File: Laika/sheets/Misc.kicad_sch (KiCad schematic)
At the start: 0 parts

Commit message: Created misc. block
Populated sheet for misc. components. This includes three switches for
SoC bringup (update, reset, arm/risc-v select). Added buzzer and user
led.
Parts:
- added BZ1: Buzzer, symbol Device:Buzzer
- added C10, C9: C, symbol Device:C
- added D4, D5, D7: D_TVS, symbol Device:D_TVS
- added D6: D, symbol Device:D
- added D8: LED, symbol Device:LED
- added Q1: Q_NPN, symbol Device:Q_NPN
- added Q2: Q_NMOS, symbol Device:Q_NMOS
- added R10, R13, R14, R8: 10k, symbol Device:R
- added R11: 180, symbol Device:R
- added R12, R7, R9: 100, symbol Device:R
- added R15, R16: 1k, symbol Device:R
- added SW1, SW2: SW_Push, symbol Switch:SW_Push
- added SW3: SW_DPDT_x2, symbol Switch:SW_DPDT_x2
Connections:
- new net: D5.2 (A2), R9.1, SW2.2
- new net: Q1.B, R11.2
- new net: BZ1.2 (-), D6.2 (A), Q1.C
- new net: R14.2, SW3.1 (A)
- new net: D7.2 (A2), R12.2, SW3.2 (B)
- new net: R13.1, SW3.3 (C)
- new net: D8.1 (K), Q2.D
- new net: Q2.G, R16.1
- new net: D4.2 (A2), R7.1, SW1.2
- new net: D8.2 (A), R15.1
- new net +1V8: R10.2, R14.1, R8.2
- new net +3V3: BZ1.1 (+), D6.1 (K), R15.2
- new net AARCH_SEL: R12.1
- new net BUZZER: R11.1
- new net GND: C10.2, C9.2, D4.1 (A1), D5.1 (A1), D7.1 (A1), Q1.E, Q2.S, R13.2, SW1.1, SW2.1
- new net RESET: C10.1, R10.1, R9.2
- new net UPDATE: C9.1, R7.2, R8.1
- new net USER_LED: R16.2
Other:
- note added: "Arm/RISC-V Switch"
- note added: "Blue PWR LED"
- note added: "Buzzer"
- note added: "Miscellaneous"
- note added: "Reset"
- note added: "USB Update Mode"
- note added: "User LED"

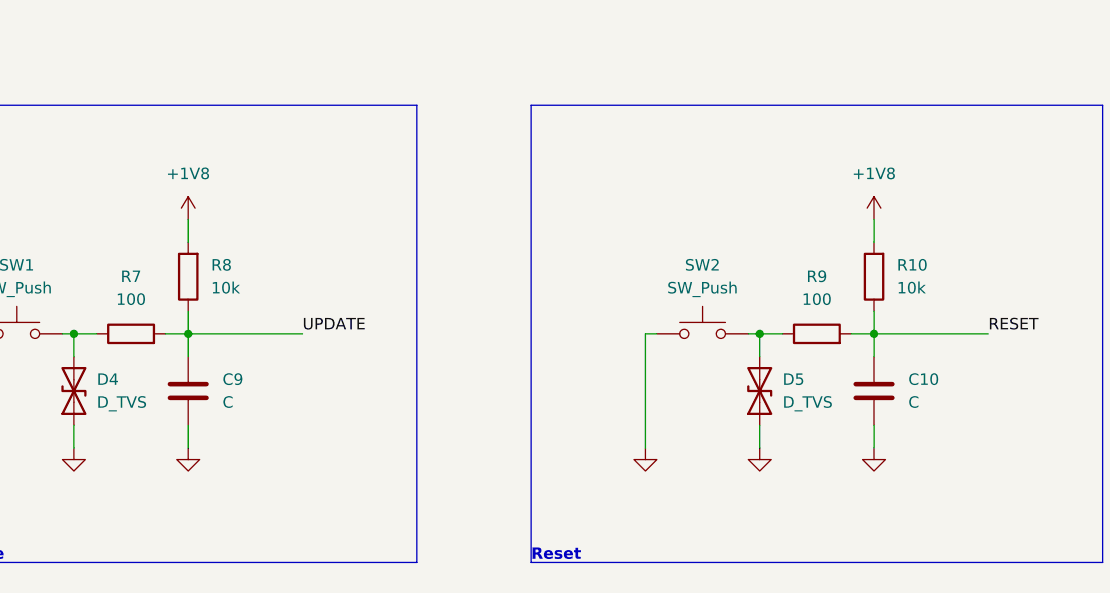
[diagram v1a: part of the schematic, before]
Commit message: Fixed reset block and added VDD_VBAT
Fixed the reset circuit to instead be pulled up to the 3v3 reg using a
voltage divider for 1.8v. RTC power (VDD_BAT) is provided by the 3v3
regulator.
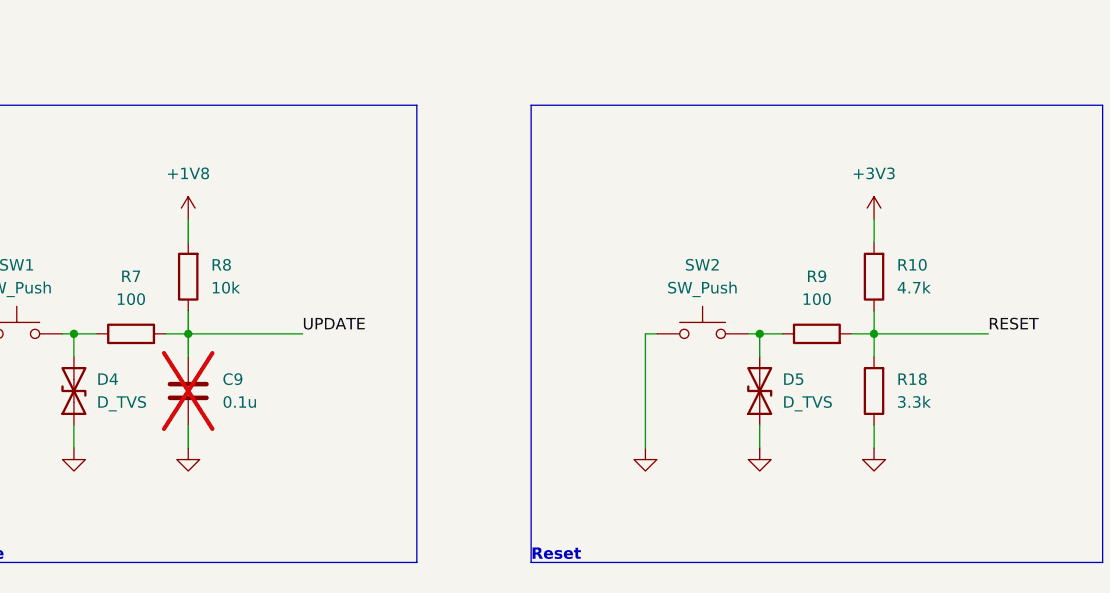
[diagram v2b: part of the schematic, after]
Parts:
- removed C10: C, symbol Device:C
- added R18: 3.3k, symbol Device:R
- C9: value C -> 0.1u; now not fitted
- R10: value 10k -> 4.7k
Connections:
- net +1V8: no longer R10.2
- net +3V3: now also R10.2
- net GND: now also R18.1
- net RESET: now also R18.2
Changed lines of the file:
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@@
 			)
 		)
-		(property "Value" "10k"
+		(property "Value" "4.7k"
 			(at 154.94 71.1199 0)
 			(effects
@@
 	)
 	(symbol
+		(lib_id "Device:R")
+		(at 152.4 82.55 180)
+		(unit 1)
+		(exclude_from_sim no)
+		(in_bom yes)
+		(on_board yes)
+		(dnp no)
+		(fields_autoplaced yes)
+		(property "Reference" "R18"
+			(at 154.94 81.2799 0)
+			(effects
+				(font
+					(size 1.27 1.27)
+				)
+				(justify right)
+			)
+		)
+		(property "Value" "3.3k"
+			(at 154.94 83.8199 0)
+			(effects
+				(font
+					(size 1.27 1.27)
+				)
+				(justify right)
+			)
+		)
+		(property "Footprint" ""
+			(at 154.178 82.55 90)
+			(effects
+				(font
+					(size 1.27 1.27)
+				)
+				(hide yes)
+			)
+		)
+		(property "Datasheet" "~"
+			(at 152.4 82.55 0)
+			(effects
+				(font
+					(size 1.27 1.27)
+				)
+				(hide yes)
+			)
+		)
+		(property "Description" "Resistor"
+			(at 152.4 82.55 0)
+			(effects
+				(font
+					(size 1.27 1.27)
+				)
+				(hide yes)
+			)
+		)
+		(pin "1"
+		)
+		(pin "2"
+		)
+		(instances
+			(project "Laika"
+				(path "/57baccbf-5d29-4714-8f2e-7e9f593fcdf8/6c078d98-f795-4bff-ba6d-ace5d579e960/048b06c9-0bbe-42fb-958a-d8b2ea4b03dd"
+					(reference "R18")
+					(unit 1)
+				)
+			)
+		)
+	)
+	(symbol
 		(lib_id "power:GND")
 		(at 63.5 88.9 0)
@@
 	)
 	(symbol
+		(lib_id "power:+3V3")
+		(at 152.4 63.5 0)
+		(unit 1)
+		(exclude_from_sim no)
+		(in_bom yes)
+		(on_board yes)
+		(dnp no)
+		(fields_autoplaced yes)
+		(property "Reference" "#PWR034"
+			(at 152.4 67.31 0)
+			(effects
+				(font
+					(size 1.27 1.27)
+				)
+				(hide yes)
+			)
+		)
+		(property "Value" "+3V3"
+			(at 152.4 58.42 0)
+			(effects
+				(font
+					(size 1.27 1.27)
+				)
+			)
+		)
+		(property "Footprint" ""
+			(at 152.4 63.5 0)
+			(effects
+				(font
+					(size 1.27 1.27)
+				)
+				(hide yes)
+			)
+		)
+		(property "Datasheet" ""
+			(at 152.4 63.5 0)
+			(effects
+				(font
+					(size 1.27 1.27)
+				)
+				(hide yes)
+			)
+		)
+		(property "Description" "Power symbol creates a global label with name \"+3V3\""
+			(at 152.4 63.5 0)
+			(effects
+				(font
+					(size 1.27 1.27)
+				)
+				(hide yes)
+			)
+		)
+		(pin "1"
+		)
+		(instances
+			(project ""
+				(path "/57baccbf-5d29-4714-8f2e-7e9f593fcdf8/6c078d98-f795-4bff-ba6d-ace5d579e960/048b06c9-0bbe-42fb-958a-d8b2ea4b03dd"
+					(reference "#PWR034")
+					(unit 1)
+				)
+			)
+		)
+	)
+	(symbol
 		(lib_id "Switch:SW_Push")
 		(at 133.35 76.2 0)
@@
 	)
 	(symbol
-		(lib_id "power:+1V8")
-		(at 152.4 63.5 0)
-		(unit 1)
-		(exclude_from_sim no)
-		(in_bom yes)
-		(on_board yes)
-		(dnp no)
-		(fields_autoplaced yes)
-		(property "Reference" "#PWR034"
-			(at 152.4 67.31 0)
-			(effects
-				(font
-					(size 1.27 1.27)
-				)
-				(hide yes)
-			)
-		)
-		(property "Value" "+1V8"
-			(at 152.4 58.42 0)
-			(effects
-				(font
-					(size 1.27 1.27)
-				)
-			)
-		)
-		(property "Footprint" ""
-			(at 152.4 63.5 0)
-			(effects
-				(font
-					(size 1.27 1.27)
-				)
-				(hide yes)
-			)
-		)
-		(property "Datasheet" ""
-			(at 152.4 63.5 0)
-			(effects
-				(font
-					(size 1.27 1.27)
-				)
-				(hide yes)
-			)
-		)
-		(property "Description" "Power symbol creates a global label with name \"+1V8\""
-			(at 152.4 63.5 0)
-			(effects
-				(font
-					(size 1.27 1.27)
-				)
-				(hide yes)
-			)
-		)
-		(pin "1"
-		)
-		(instances
-			(project "Laika"
-				(path "/57baccbf-5d29-4714-8f2e-7e9f593fcdf8/6c078d98-f795-4bff-ba6d-ace5d579e960/048b06c9-0bbe-42fb-958a-d8b2ea4b03dd"
-					(reference "#PWR034")
-					(unit 1)
-				)
-			)
-		)
-	)
-	(symbol
 		(lib_id "Device:C")
 		(at 76.2 82.55 0)
@@
 		(in_bom yes)
 		(on_board yes)
-		(dnp no)
+		(dnp yes)
 		(fields_autoplaced yes)
 		(property "Reference" "C9"
@@
 			)
 		)
-		(property "Value" "C"
+		(property "Value" "0.1u"
 			(at 80.01 83.8199 0)
 			(effects
@@
 					(unit 1)
 				)
-			)
-		)
-	)
-	(symbol
-		(lib_id "Device:C")
-		(at 152.4 82.55 0)
-		(unit 1)
-		(exclude_from_sim no)
-		(in_bom yes)
-		(on_board yes)
-		(dnp no)
-		(fields_autoplaced yes)
-		(property "Reference" "C10"
-			(at 156.21 81.2799 0)
-			(effects
-				(font
-					(size 1.27 1.27)
-				)
-				(justify left)
-			)
-		)
-		(property "Value" "C"
-			(at 156.21 83.8199 0)
-			(effects
-				(font
-					(size 1.27 1.27)
-				)
-				(justify left)
-			)
-		)
-		(property "Footprint" ""
-			(at 153.3652 86.36 0)
-			(effects
-				(font
-					(size 1.27 1.27)
-				)
-				(hide yes)
-			)
-		)
-		(property "Datasheet" "~"
-			(at 152.4 82.55 0)
-			(effects
-				(font
-					(size 1.27 1.27)
-				)
-				(hide yes)
-			)
-		)
-		(property "Description" "Unpolarized capacitor"
-			(at 152.4 82.55 0)
-			(effects
-				(font
-					(size 1.27 1.27)
-				)
-				(hide yes)
-			)
-		)
-		(pin "1"
-		)
-		(pin "2"
-		)
-		(instances
-			(project "Laika"
-				(path "/57baccbf-5d29-4714-8f2e-7e9f593fcdf8/6c078d98-f795-4bff-ba6d-ace5d579e960/048b06c9-0bbe-42fb-958a-d8b2ea4b03dd"
-					(reference "C10")
-					(unit 1)
-				)

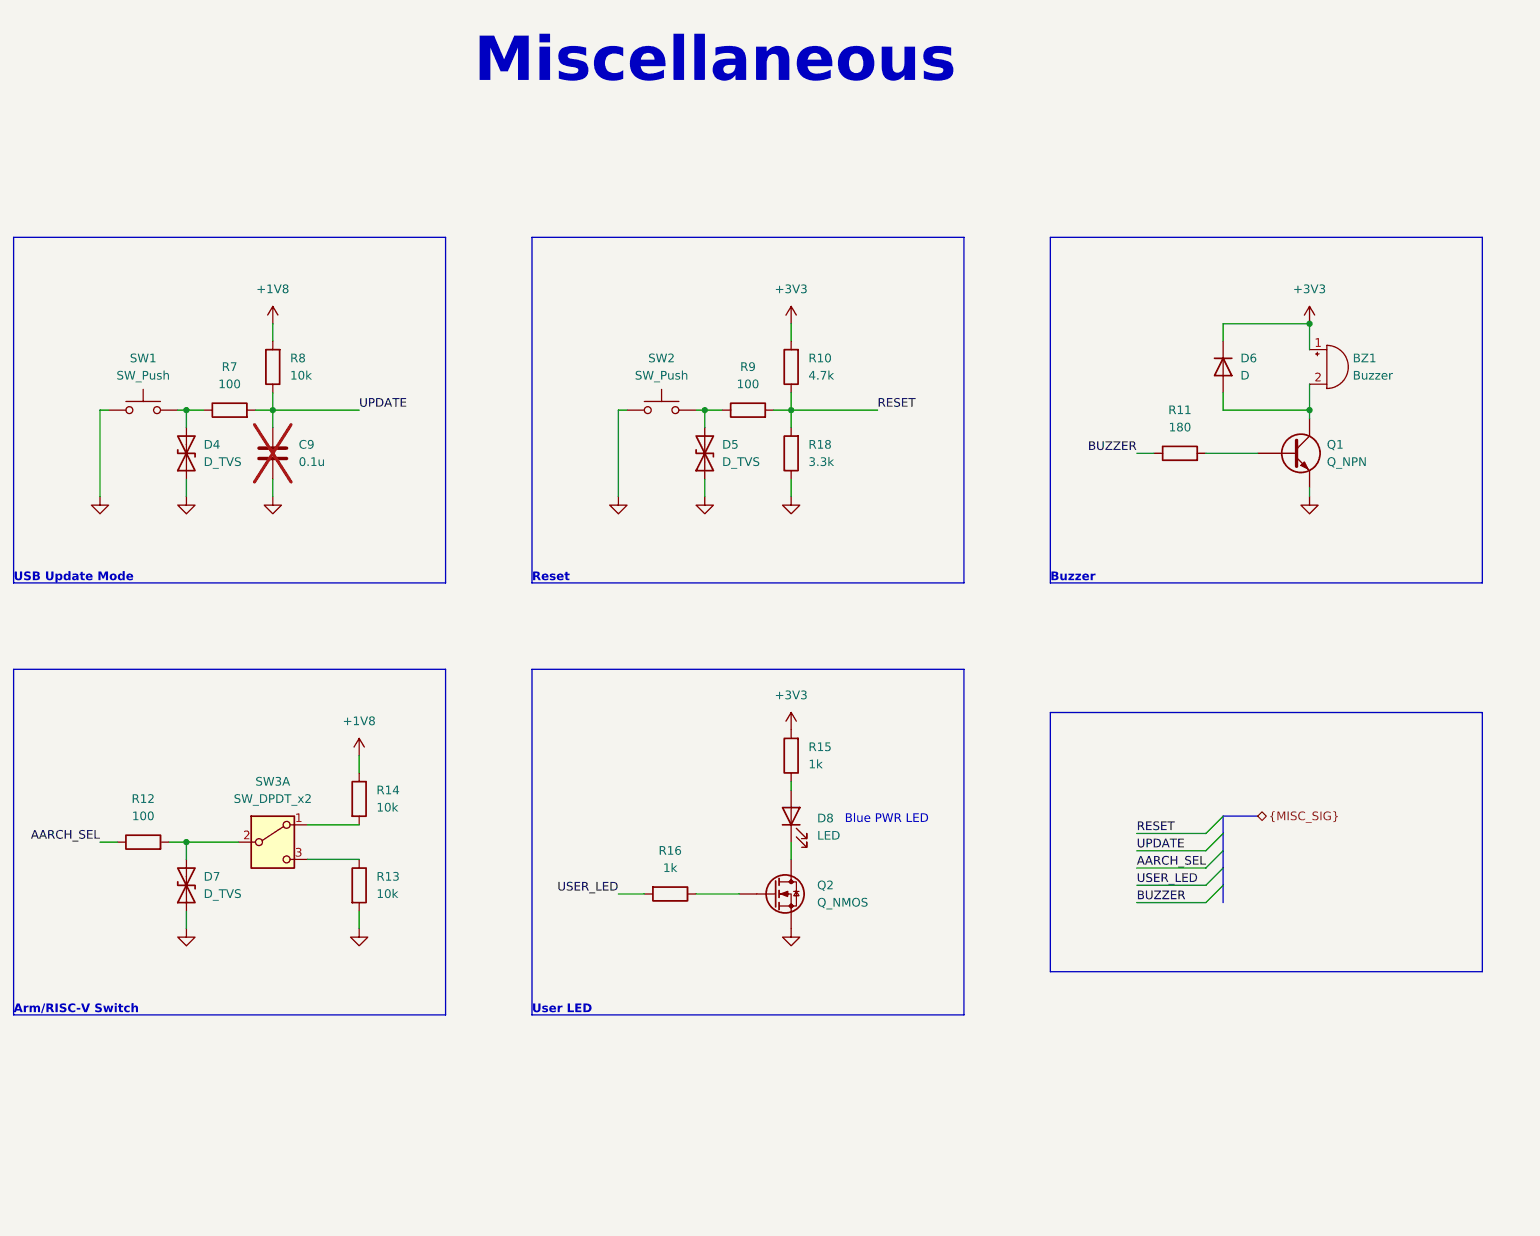
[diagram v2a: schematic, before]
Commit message: Populated BOM with part numbers and footprints
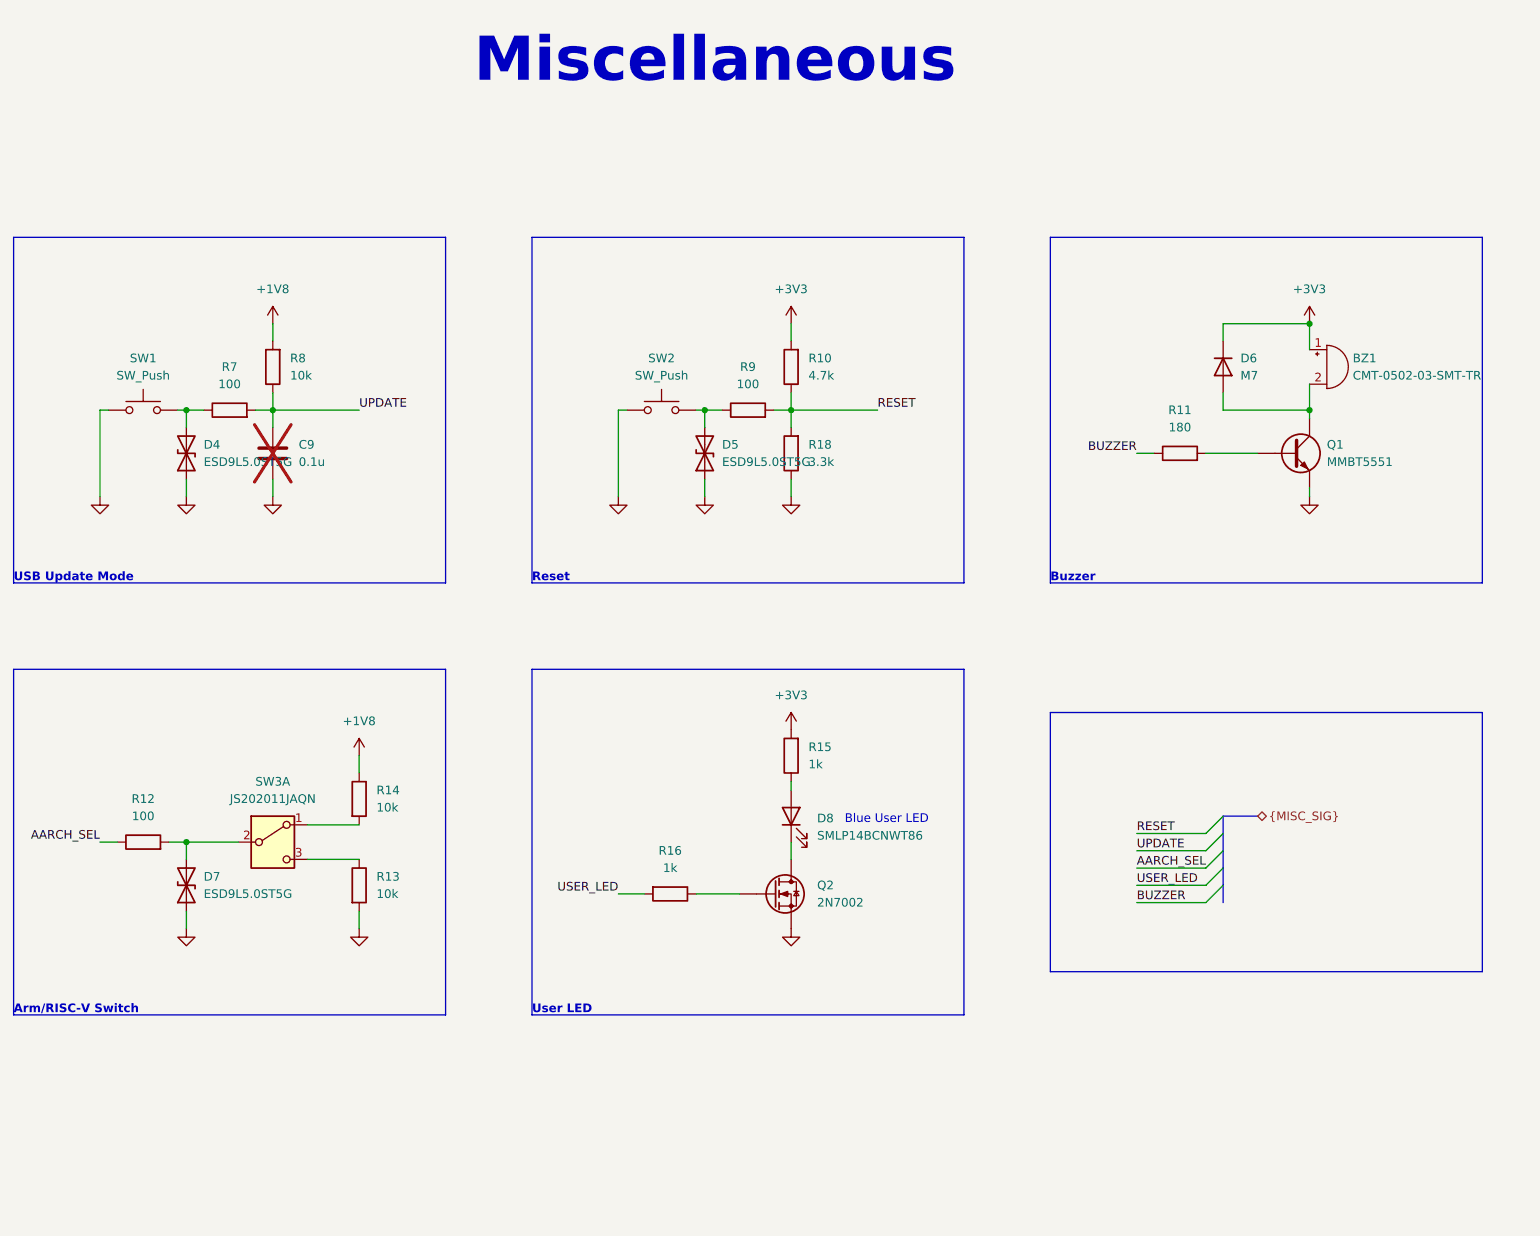
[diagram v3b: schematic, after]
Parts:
- BZ1: value Buzzer -> CMT-0502-03-SMT-TR; Manafacturer (none) -> Same Sky; Part Number (none) -> CMT-0502-03-SMT-TR
- C9: footprint (none) -> Capacitor_SMD:C_0402_1005Metric; JLC Part Type (none) -> Basic; Manafacturer (none) -> Samsung Electro-Mechanics; Part Number (none) -> CL05B104KO5NNNC
- D4, D5, D7: value D_TVS -> ESD9L5.0ST5G; footprint (none) -> Diode_SMD:D_SOD-923; JLC Part Type (none) -> Extended; Manafacturer (none) -> onsemi; Part Number (none) -> ESD9L5.0ST5G
- D6: value D -> M7; footprint (none) -> Diode_SMD:D_SMA; JLC Part Type (none) -> Basic; Manafacturer (none) -> Diotec Semiconductor; Part Number (none) -> M7
- D8: value LED -> SMLP14BCNWT86; footprint (none) -> LED_SMD:LED_0402_1005Metric; JLC Part Type (none) -> Extended; Manafacturer (none) -> Rohm Semiconductor; Part Number (none) -> SMLP14BCNWT86
- Q1: value Q_NPN -> MMBT5551; footprint (none) -> Package_TO_SOT_SMD:SOT-23; JLC Part Type (none) -> Basic; Manafacturer (none) -> Diotec Semiconductor; Part Number (none) -> MMBT5551
- Q2: value Q_NMOS -> 2N7002; footprint (none) -> Package_TO_SOT_SMD:SOT-23-3; JLC Part Type (none) -> Basic; Manafacturer (none) -> onsemi / Fairchild; Part Number (none) -> 2N7002
- R10: footprint (none) -> Resistor_SMD:R_0402_1005Metric_Pad0.72x0.64mm_HandSolder; JLC Part Type (none) -> Basic; Manafacturer (none) -> Royalohm; Part Number (none) -> 0402WGF4701TCE
- R11: footprint (none) -> Resistor_SMD:R_0402_1005Metric_Pad0.72x0.64mm_HandSolder; JLC Part Type (none) -> Basic; Manafacturer (none) -> Royalohm; Part Number (none) -> 0402WGJ0181TCE
- R12, R7, R9: footprint (none) -> Resistor_SMD:R_0402_1005Metric_Pad0.72x0.64mm_HandSolder; JLC Part Type (none) -> Basic; Manafacturer (none) -> Royalohm; Part Number (none) -> 0402WGF1000TCE
- R13, R14, R8: footprint (none) -> Resistor_SMD:R_0402_1005Metric_Pad0.72x0.64mm_HandSolder; JLC Part Type (none) -> Basic; Manafacturer (none) -> Royalohm; Part Number (none) -> 0402WGJ0103TCE
- R15, R16: footprint (none) -> Resistor_SMD:R_0402_1005Metric_Pad0.72x0.64mm_HandSolder; JLC Part Type (none) -> Basic; Manafacturer (none) -> Royalohm; Part Number (none) -> 0402WGF1001TCE
- R18: footprint (none) -> Resistor_SMD:R_0402_1005Metric_Pad0.72x0.64mm_HandSolder; JLC Part Type (none) -> Basic; Manafacturer (none) -> Royalohm; Part Number (none) -> 0402WGF3301TCE
- SW1, SW2: JLC Part Type (none) -> Extended; Manafacturer (none) -> C&K; Part Number (none) -> KMR211GLFS
- SW3: value SW_DPDT_x2 -> JS202011JAQN; footprint (none) -> Button_Switch_THT:SW_CK_JS202011AQN_DPDT_Angled; JLC Part Type (none) -> Extended; Manafacturer (none) -> C&K; Part Number (none) -> JS202011JAQN
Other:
- note added: "Blue User LED"
- note removed: "Blue PWR LED"

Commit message: Added footprint for buzzer
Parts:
- BZ1: footprint (none) -> CMT-0502-03-SMT-TR:XDCR_CMT-0502-03-SMT-TR
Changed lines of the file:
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@@
 			)
 		)
-		(property "Footprint" ""
+		(property "Footprint" "CMT-0502-03-SMT-TR:XDCR_CMT-0502-03-SMT-TR"
 			(at 230.505 67.31 90)
 			(effects

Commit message: Added footprint for push buttons
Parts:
- SW1, SW2: footprint (none) -> Button_Switch_SMD:SW_Push_1P1T_NO_CK_KMR2
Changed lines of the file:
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@@
 			)
 		)
-		(property "Footprint" ""
+		(property "Footprint" "Button_Switch_SMD:SW_Push_1P1T_NO_CK_KMR2"
 			(at 133.35 71.12 0)
 			(effects
@@
 			)
 		)
-		(property "Footprint" ""
+		(property "Footprint" "Button_Switch_SMD:SW_Push_1P1T_NO_CK_KMR2"
 			(at 57.15 71.12 0)
 			(effects

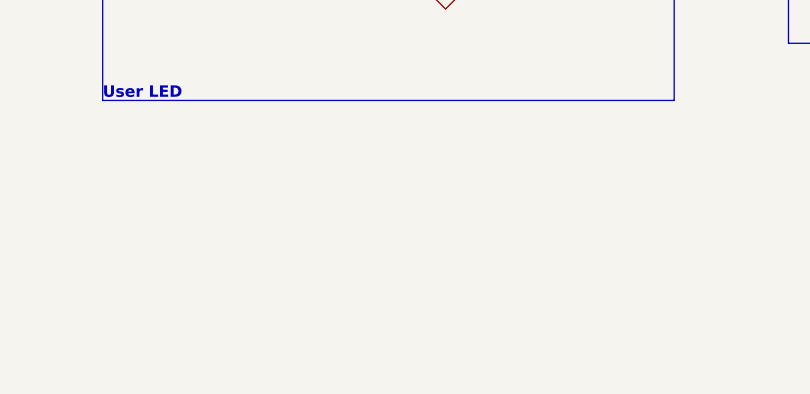
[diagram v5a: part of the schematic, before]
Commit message: Added mounting holes
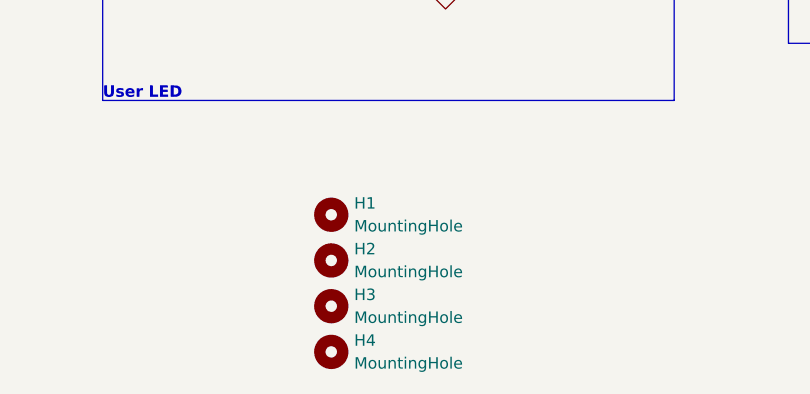
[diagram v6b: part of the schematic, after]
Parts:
- added H1, H2, H3, H4: MountingHole, MountingHole:MountingHole_2.2mm_M2_DIN965_Pad, symbol Mechanical:MountingHole
